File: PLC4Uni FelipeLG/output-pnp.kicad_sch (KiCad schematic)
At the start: 3 parts, among them Q7 2SA2018

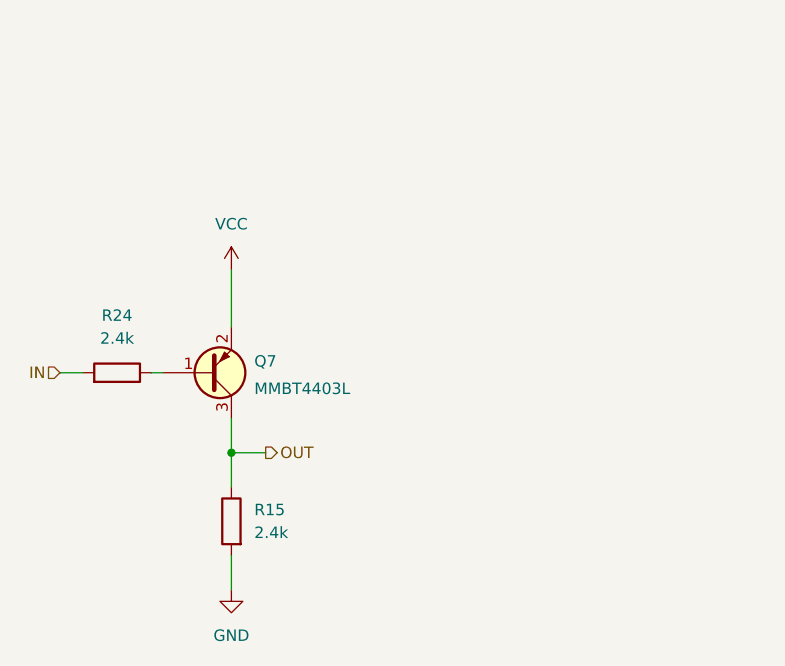
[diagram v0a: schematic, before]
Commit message: Add files via upload
Updated Circuitos corregidos y pistas agregadas
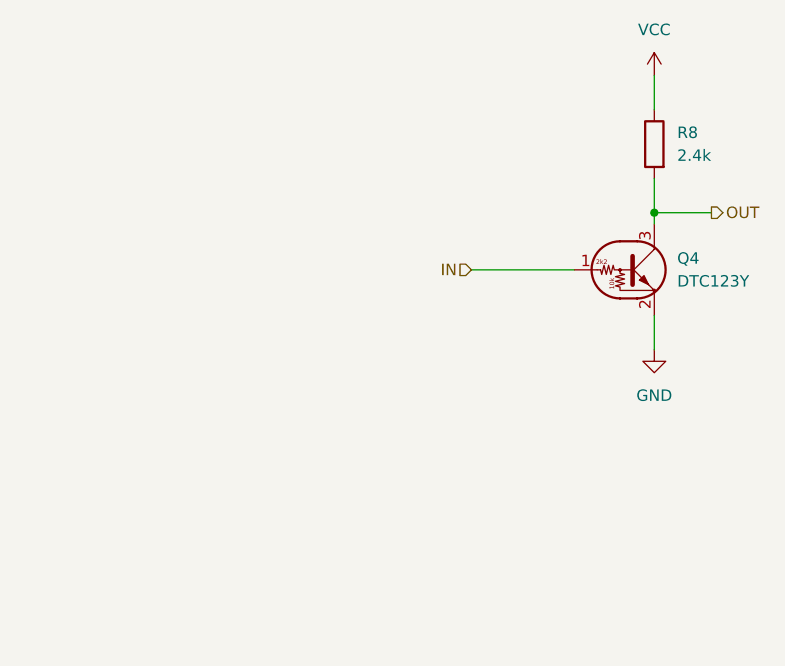
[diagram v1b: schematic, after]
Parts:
- removed Q7: 2SA2018, Package_TO_SOT_SMD_AKL:SOT-416, symbol Transistor_BJT_AKL:2SA2018
- removed R15, R24: 2.4k, Resistor_SMD_AKL:R_0603_1608Metric, symbol Resistor_AKL:R_0603
- added Q4: DTC123Y, Package_TO_SOT_SMD:SOT-23, symbol Transistor_BJT:DTC123Y
- added R8: 2.4k, Resistor_SMD_AKL:R_0603_1608Metric, symbol Resistor_AKL:R_0603
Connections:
- net GND: now also Q4.2 (E)
- net IN: now also Q4.1 (B)
- net OUT: now also Q4.3 (C), R8.1
- net VCC: now also R8.2
